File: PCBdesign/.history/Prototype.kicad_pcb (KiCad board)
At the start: 2 copper layers, 15 parts, among them J1 AudioJack2, J2 Adafruit Micro-Lipo, SW2 SW_Nidec_CAS-120A1, U1 ESP32-S3-WROOM-2, U2 ER_OLEDM0.91_1x-I2C, U3 AP2112K-3.3, U4 MAX98357A, U5 PCM5102A

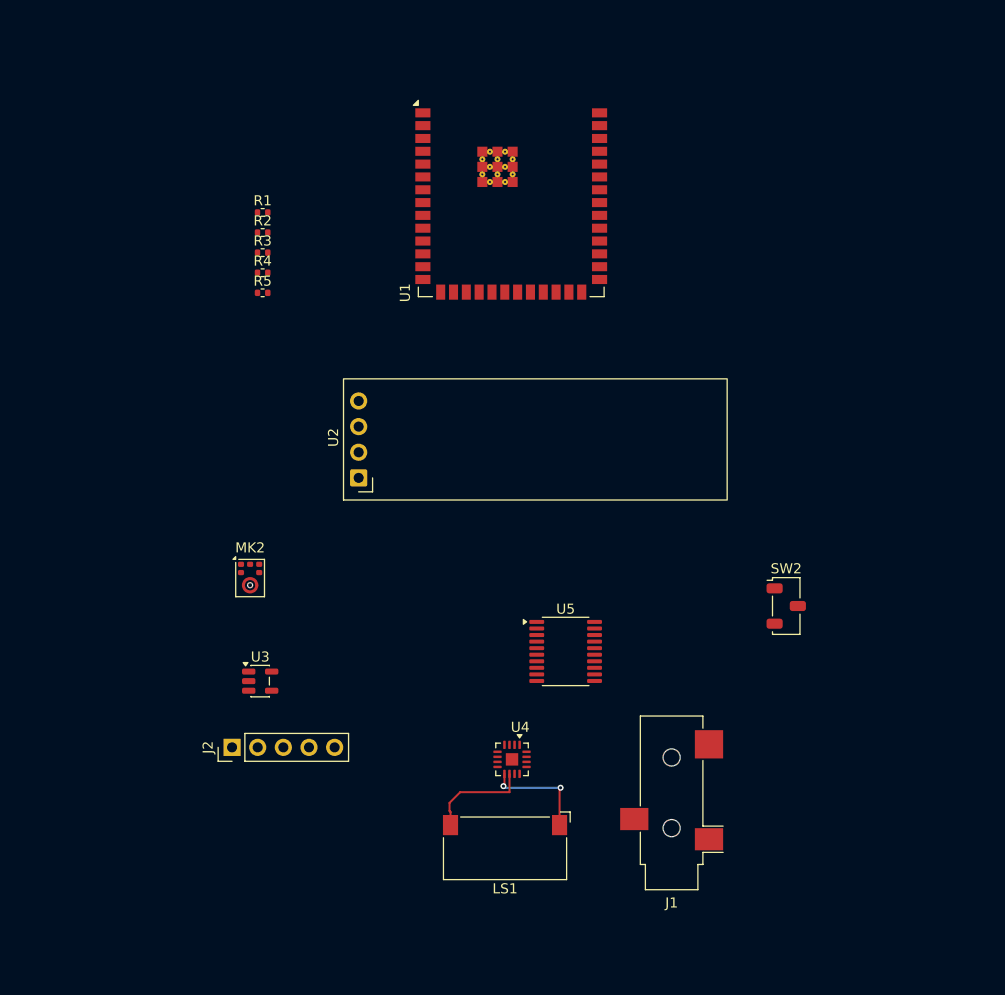
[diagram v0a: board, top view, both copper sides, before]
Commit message: Update PCB layout and schematic fixes
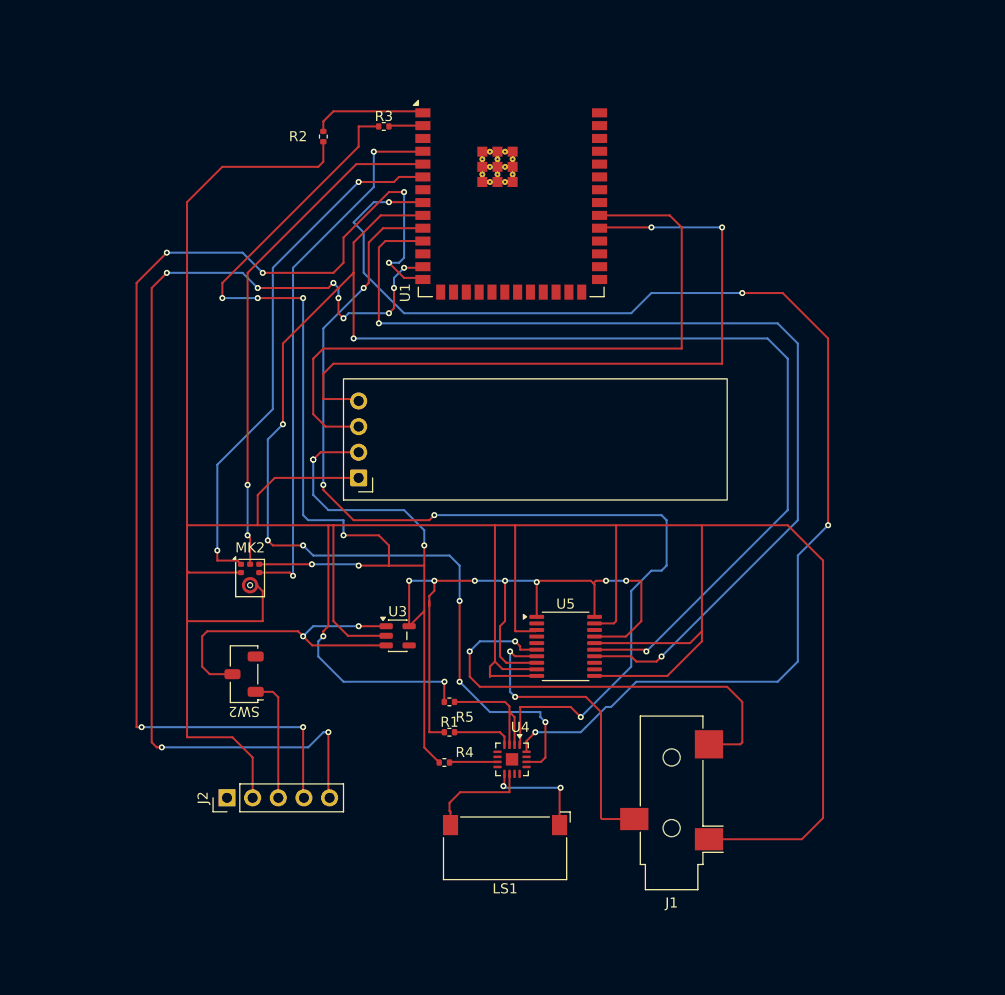
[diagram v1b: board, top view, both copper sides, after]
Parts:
- moved R1 54.7 mm to (125.5, 81.5)
- moved SW2 54.1 mm to (105.2, 75.8), turned to 180 degrees
- moved R4 51.7 mm to (125.0, 84.5), turned to 180 degrees
- moved R5 44.5 mm to (125.5, 78.5), turned to 180 degrees
- moved R3 17.3 mm to (119.0, 21.5), turned to 180 degrees
- moved U3 14.3 mm to (120.4, 72.0)
- moved R2 11.2 mm to (113.0, 22.5), turned to 90 degrees
- moved J2 5.02 mm to (103.5, 88.0)
- moved U5 0.50 mm to (137.0, 73.0)
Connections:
- J1 pad S: Net-(J2-GND) -> Net-(MK2-GND)
- MK2 pad 2: Net-(J2-GND) -> Net-(MK2-GND)
- MK2 pad 3: Net-(J2-GND) -> Net-(MK2-GND)
- R3 pad 1: Net-(U2-VCC) -> Net-(MK2-VDD)
- R4 pad 2: Net-(U2-VCC) -> Net-(MK2-VDD)
- R5 pad 1: Net-(J2-GND) -> Net-(MK2-GND)
- SW2 pad 1: Net-(J2-BAT) -> Net-(SW2-C)
- SW2 pad 2: Net-(MK2-VDD) -> Net-(SW2-B)
- U1 pad 13: Net-(J2-D-) -> Net-(U1-USB_D-/IO19)
- U1 pad 14: Net-(J2-D+) -> Net-(U1-USB_D+/IO20)
- U2 pad 1: Net-(J2-GND) -> Net-(MK2-GND)
- U2 pad 2: Net-(U2-VCC) -> Net-(MK2-VDD)
- U3 pad 1: Net-(MK2-VDD) -> Net-(SW2-B)
- U3 pad 2: Net-(J2-GND) -> Net-(MK2-GND)
- U3 pad 3: Net-(MK2-VDD) -> Net-(SW2-B)
- U3 pad 5: Net-(U2-VCC) -> Net-(MK2-VDD)
- U5 pad 10: Net-(J2-GND) -> Net-(MK2-GND)
- U5 pad 11: Net-(J2-GND) -> Net-(MK2-GND)
- U5 pad 16: Net-(J2-GND) -> Net-(MK2-GND)
- U5 pad 19: Net-(J2-GND) -> Net-(MK2-GND)
- U5 pad 3: Net-(J2-GND) -> Net-(MK2-GND)
- U5 pad 9: Net-(J2-GND) -> Net-(MK2-GND)
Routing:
- net Net-(U4-GAIN_SLOT): track 0.00 -> 354.6 mm, vias 0 -> 2
- net Net-(U1-IO16): track 0.00 -> 178.9 mm, vias 0 -> 8
- net Net-(MK2-VDD): track 0.00 -> 156.2 mm, vias 0 -> 16
- net Net-(U1-IO15): track 0.00 -> 127.9 mm, vias 0 -> 4
- net Net-(U1-USB_D+/IO20): track 0.00 -> 113.1 mm, vias 0 -> 6
- net Net-(U1-USB_D-/IO19): track 0.00 -> 105.0 mm, vias 0 -> 10
- net Net-(U1-IO17): track 0.00 -> 101.8 mm, vias 0 -> 4
- net Net-(U1-IO18): track 0.00 -> 98.1 mm, vias 0 -> 2
- net Net-(U1-IO38): track 0.00 -> 71.7 mm, vias 0 -> 2
- net Net-(U1-MTCK/IO39): track 0.00 -> 68.1 mm
- net Net-(MK2-BCLK): track 0.00 -> 53.7 mm, vias 0 -> 2
- net Net-(MK2-WS): track 0.00 -> 52.4 mm, vias 0 -> 2
- net Net-(MK2-DATA): track 0.00 -> 50.8 mm, vias 0 -> 2
- net (no net): track 0.00 -> 46.5 mm
- net Net-(U5-OUTL): track 0.00 -> 45.5 mm, vias 0 -> 2
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
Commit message: Describe your updates here
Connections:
- R3 pad 1: Net-(MK2-VDD) -> Net-(U2-VCC)
- R4 pad 2: Net-(MK2-VDD) -> Net-(U2-VCC)
- SW2 pad 2: Net-(SW2-B) -> Net-(MK2-VDD)
- U2 pad 2: Net-(MK2-VDD) -> Net-(U2-VCC)
- U3 pad 1: Net-(SW2-B) -> Net-(MK2-VDD)
- U3 pad 3: Net-(SW2-B) -> Net-(MK2-VDD)
- U3 pad 5: Net-(MK2-VDD) -> Net-(U2-VCC)
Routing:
- net Net-(J2-GND): track 0.00 -> 324.0 mm
- net Net-(U4-GAIN_SLOT): track 354.6 -> 30.6 mm
- net (no net): track 46.5 -> 0.00 mm
- net Net-(U2-VCC): track 0.00 -> 45.9 mm, vias 0 -> 3
- net Net-(SW2-B): track 34.0 -> 0.00 mm, vias 2 -> 0
- net Net-(MK2-VDD): track 156.2 -> 190.2 mm, vias 16 -> 15

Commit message: New files
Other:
- board outline added: 95.5 x 92.5 mm
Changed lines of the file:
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@@
 			(outputformat 1)
 			(mirror no)
-			(drillshape 1)
+			(drillshape 0)
 			(scaleselection 1)
-			(outputdirectory "")
+			(outputdirectory "./")
 		)
 	)
@@
 		)
 	)
+	(gr_rect
+		(start 83 11)
+		(end 178.5 103.5)
+		(stroke
+			(width 0.05)
+			(type default)
+		)
+		(fill no)
+		(layer "Edge.Cuts")
+	)
 	(segment

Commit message: Replace specific folders while keeping external files
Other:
- board size 95.5 x 92.5 mm -> 71.5 x 93.5 mm
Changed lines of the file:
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@@
 		(tags "TQFN NoLead")
 		(property "Reference" "U4"
-			(at -3.19 -0.81 180)
+			(at -3.19 -0.81 0)
 			(layer "F.SilkS")
 			(effects
@@
 		)
 		(property "Value" "MAX98357A"
-			(at -4.69 -0.81 180)
+			(at -4.69 -0.81 0)
 			(layer "F.Fab")
 			(effects
@@
 		(embedded_fonts no)
 		(model "${KICAD10_3DMODEL_DIR}/Package_DFN_QFN.3dshapes/TQFN-16-1EP_3x3mm_P0.5mm_EP1.23x1.23mm.step"
+			(hide yes)
 			(offset
 				(xyz 0 0 0)
@@
 			)
 		)
+		(model "${KIPRJMOD}/MAX98357AETE+T.STEP"
+			(offset
+				(xyz 0 0 0)
+			)
+			(scale
+				(xyz 1 1 1)
+			)
+			(rotate
+				(xyz 90 -180 -180)
+			)
+		)
 	)
 	(footprint "RF_Module:ESP32-S3-WROOM-2"
@@
 		(embedded_fonts no)
 		(model "${KICAD10_3DMODEL_DIR}/Button_Switch_SMD.3dshapes/Nidec_Copal_CAS-120A.step"
+			(hide yes)
+			(offset
+				(xyz 0 0 0)
+			)
+			(scale
+				(xyz 1 1 1)
+			)
+			(rotate
+				(xyz 0 0 0)
+			)
+		)
+		(model "${KIPRJMOD}/OLED 128 x 32 Display Assembly.step"
+			(hide yes)
 			(offset
 				(xyz 0 0 0)
@@
 			)
 		)
+		(model "${KIPRJMOD}/User Library-cas-120a1.STEP"
+			(offset
+				(xyz 0 0 0)
+			)
+			(scale
+				(xyz 1 1 1)
+			)
+			(rotate
+				(xyz -90 -0 90)
+			)
+		)
 	)
 	(footprint "Resistor_SMD:R_0402_1005Metric"
@@
 		(embedded_fonts no)
 		(model "${KICAD10_3DMODEL_DIR}/Connector_Audio.3dshapes/Jack_3.5mm_CUI_SJ-3523-SMT_Horizontal.step"
+			(hide yes)
 			(offset
 				(xyz 0 0 0)
@@
 			)
 		)
+		(model "${KIPRJMOD}/SJ-3523-SMT-TR--3DModel-STEP-1.STEP"
+			(offset
+				(xyz 0 6 2.5)
+			)
+			(scale
+				(xyz 1 1 1)
+			)
+			(rotate
+				(xyz 90 -180 -0)
+			)
+		)
 	)
 	(footprint "Resistor_SMD:R_0402_1005Metric"
@@
 		(model "${KICAD10_3DMODEL_DIR}/Connector_PinHeader_2.54mm.3dshapes/PinHeader_1x05_P2.54mm_Vertical.step"
 			(offset
-				(xyz 0 0 0)
+				(xyz 0 0 1.5)
 			)
 			(scale
@@
 			)
 			(rotate
-				(xyz 0 0 0)
+				(xyz -0 -0 -0)
+			)
+		)
+		(model "${KIPRJMOD}/4410 Micro Lipo USBC.step"
+			(offset
+				(xyz -17 5.5 0)
+			)
+			(scale
+				(xyz 1 1 1)
+			)
+			(rotate
+				(xyz -0 -0 90)
 			)
 		)
@@
 		(embedded_fonts no)
 		(model "${KICAD10_3DMODEL_DIR}/Display.3dshapes/ER_OLEDM0.91_1x-I2C.step"
+			(hide yes)
 			(offset
 				(xyz 0 0 0)
@@
 			)
 		)
+		(model "${KIPRJMOD}/OLED 128 x 32 Display Assembly.step"
+			(offset
+				(xyz 4 -16.5 0)
+			)
+			(scale
+				(xyz 1 1 1)
+			)
+			(rotate
+				(xyz -0 -0 90)
+			)
+		)
 	)
 	(footprint "Resistor_SMD:R_0402_1005Metric"
@@
 	)
 	(gr_rect
-		(start 83 11)
-		(end 178.5 103.5)
+		(start 93 12)
+		(end 164.5 105.5)
 		(stroke
 			(width 0.05)
